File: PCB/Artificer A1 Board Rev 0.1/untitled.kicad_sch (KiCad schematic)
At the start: 3 parts

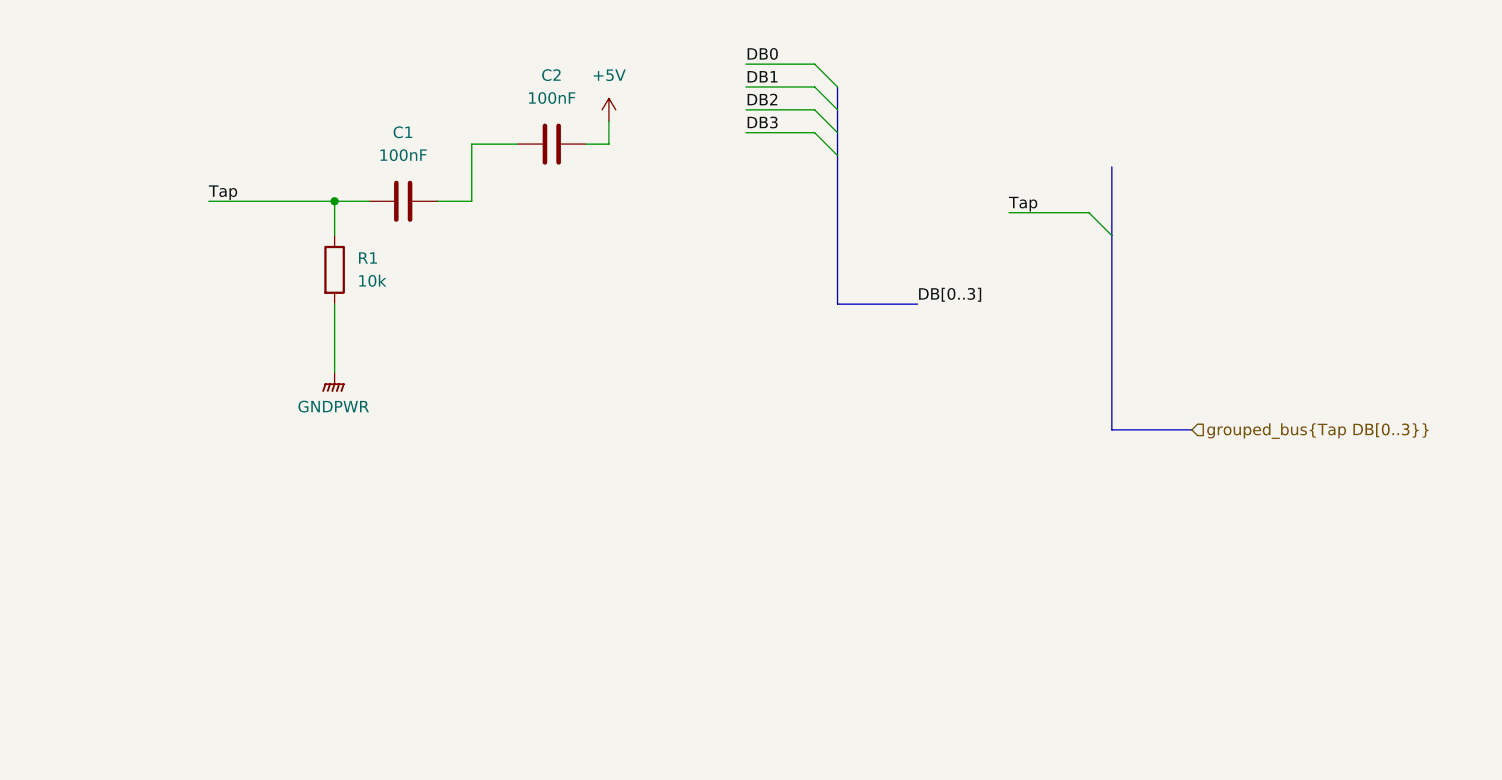
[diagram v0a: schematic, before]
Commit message: cleaned up, kicad 10 & usb c pd
migrated to Kicad 10,
added USB PD for power input
added capacitors inductors and resistor footprints
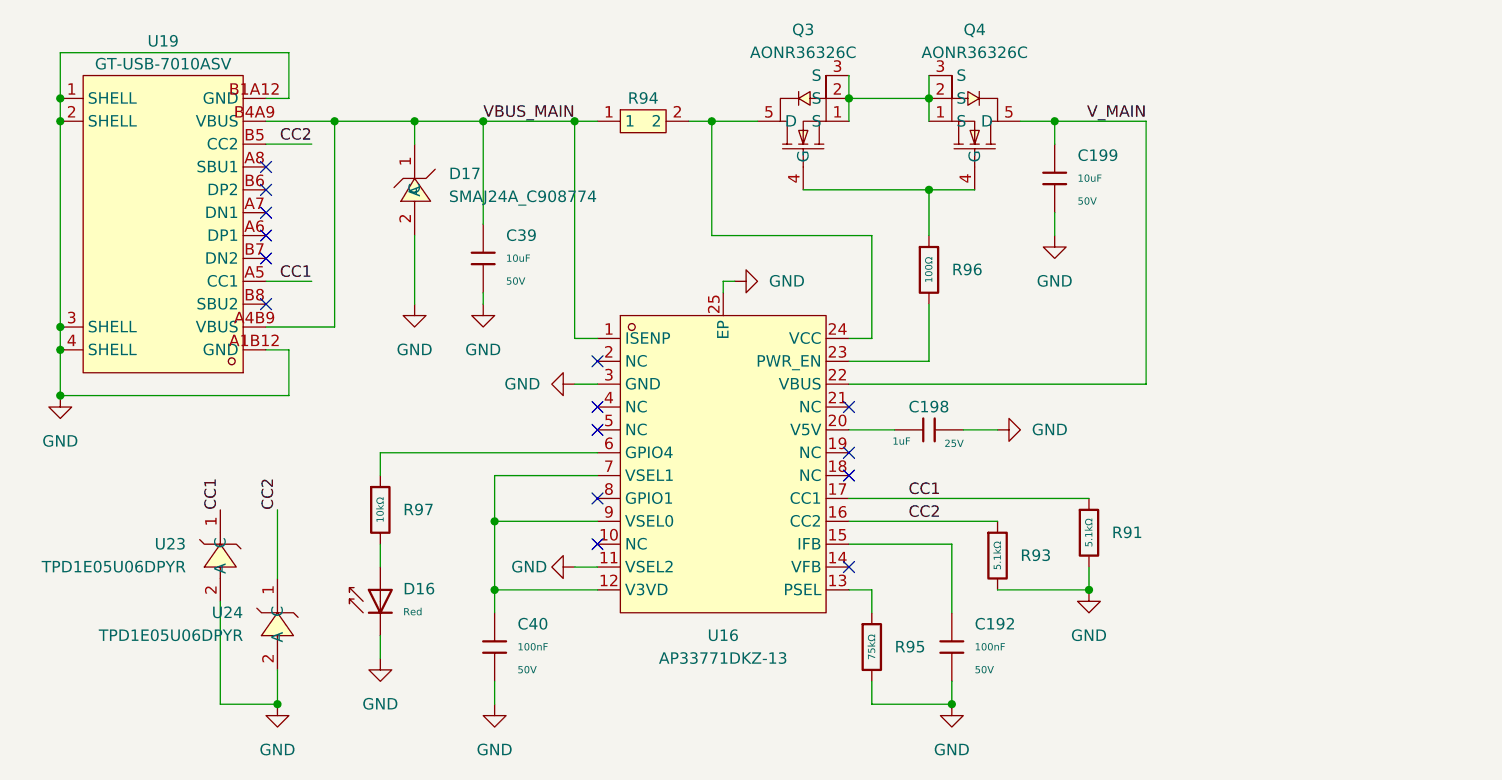
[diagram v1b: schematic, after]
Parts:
- removed C1, C2: 100nF, symbol Device:C
- removed R1: 10k, symbol Device:R
- added C192, C40: 100nF, PCM_JLCPCB:C_0402, symbol PCM_JLCPCB-Capacitors:0402,100nF,(2)
- added C198: 1uF, PCM_JLCPCB:C_0402, symbol PCM_JLCPCB-Capacitors:0402,1uF
- added C199, C39: 10uF, PCM_JLCPCB:C_0805, symbol PCM_JLCPCB-Capacitors:0805,10uF,(2)
- added D16: Red, PCM_JLCPCB:D_0603, symbol PCM_JLCPCB-Diodes:LED,0603,Red
- added D17: SMAJ24A_C908774, easyeda:SMA_L4.3-W2.7-LS5.1-RD, symbol easyeda:SMAJ24A_C908774
- added Q3, Q4: AONR36326C, easyeda:DFN-8_L3.3-W3.3-P0.65-BL, symbol easyeda:AONR36326C
- added R91, R93: 5.1kΩ, PCM_JLCPCB:R_0402, symbol PCM_JLCPCB-Resistors:0402,5.1kΩ
- added R94: JER1206F1R010, easyeda:R1206, symbol easyeda:JER1206F1R010
- added R95: 75kΩ, PCM_JLCPCB:R_0402, symbol PCM_JLCPCB-Resistors:0402,75kΩ
- added R96: 100Ω, PCM_JLCPCB:R_0402, symbol PCM_JLCPCB-Resistors:0402,100Ω
- added R97: 10kΩ, PCM_JLCPCB:R_0402, symbol PCM_JLCPCB-Resistors:0402,10kΩ
- added U16: AP33771DKZ-13, easyeda:WQFN-24_L4.0-W4.0-P0.50-TL-EP2.7, symbol easyeda:AP33771DKZ-13
- added U19: GT-USB-7010ASV, easyeda:USB-C-SMD_G-SWITCH_GT-USB-7010ASV, symbol easyeda:GT-USB-7010ASV
- added U23, U24: TPD1E05U06DPYR, easyeda:DFN1006-2L-RD, symbol easyeda:TPD1E05U06DPYR_C2937017
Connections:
- new net: C198.1, U16.20 (V5V)
- new net: C192.1, U16.15 (IFB)
- new net: Q3.5 (D), R94.2, U16.24 (VCC)
- new net: R97.1, U16.6 (GPIO4)
- new net: D16.2, R97.2
- new net: Q3.1 (S), Q3.2 (S), Q3.3 (S), Q4.1 (S), Q4.2 (S), Q4.3 (S)
- new net: Q3.4 (G), Q4.4 (G), R96.1
- new net: R95.1, U16.13 (PSEL)
- new net: C40.1, U16.12 (V3VD), U16.7 (VSEL1), U16.9 (VSEL0)
- new net: R96.2, U16.23 (PWR_EN)
- new net CC1: R91.1, U16.17 (CC1), U19.A5 (CC1), U23.1 (C)
- new net CC2: R93.1, U16.16 (CC2), U19.B5 (CC2), U24.1 (C)
- new net GND: C192.2, C198.2, C199.2, C39.2, C40.2, D16.1, D17.2 (A), R91.2, R93.2, R95.2, U16.11 (VSEL2), U16.25 (EP), U16.3 (GND), U19.1 (SHELL), U19.2 (SHELL), U19.3 (SHELL), U19.4 (SHELL), U19.A1B12 (GND), U19.B1A12 (GND), U23.2 (A), U24.2 (A)
- new net VBUS_MAIN: C39.1, D17.1 (C), R94.1, U16.1 (ISENP), U19.A4B9 (VBUS), U19.B4A9 (VBUS)
- new net V_MAIN: C199.1, Q4.5 (D), U16.22 (VBUS)
- no-connect marks 0 -> 15
